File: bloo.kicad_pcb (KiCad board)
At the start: 2 copper layers, 0 parts

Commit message: feat: create PCB shape and motor placement
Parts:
- added BT1: Battery_Cell, Connector_AMASS:AMASS_XT30UPB-M_1x02_P5.0mm_Vertical, F.Cu at (27.0, 155.0)
- added BT_MH1: M2, MountingHole:MountingHole_2.2mm_M2, F.Cu at (112.9, 187.9)
- added BT_MH2: M2, MountingHole:MountingHole_2.2mm_M2, F.Cu at (112.9, 193.8)
- added BT_MH3: M2, MountingHole:MountingHole_2.2mm_M2, F.Cu at (118.5, 187.9)
- added BT_MH4: M2, MountingHole:MountingHole_2.2mm_M2, F.Cu at (118.9, 193.8)
- added C1: 0.1uF, Capacitor_SMD:C_1206_3216Metric_Pad1.33x1.80mm_HandSolder, F.Cu at (375.0, 47.8)
- added C10: 10uF(Tantalum), Capacitor_SMD:C_1206_3216Metric_Pad1.33x1.80mm_HandSolder, F.Cu at (375.0, 61.2)
- added C11: 10uF, Capacitor_SMD:C_1206_3216Metric_Pad1.33x1.80mm_HandSolder, F.Cu at (375.0, 64.6)
- added C12: 0.1uF, Capacitor_SMD:C_1206_3216Metric_Pad1.33x1.80mm_HandSolder, F.Cu at (381.0, 47.8)
- added C13: 0.1uF, Capacitor_SMD:C_1206_3216Metric_Pad1.33x1.80mm_HandSolder, F.Cu at (381.0, 51.2)
- added C14: 1uF, Capacitor_SMD:C_1206_3216Metric_Pad1.33x1.80mm_HandSolder, F.Cu at (381.0, 54.5)
- added C15: 1uF, Capacitor_SMD:C_1206_3216Metric_Pad1.33x1.80mm_HandSolder, F.Cu at (381.0, 57.9)
- added C16: 100uF, Capacitor_THT:CP_Radial_D6.3mm_P2.50mm, F.Cu at (39.3, 255.5)
- added C17: 1uF, Capacitor_SMD:C_1206_3216Metric_Pad1.33x1.80mm_HandSolder, F.Cu at (381.0, 61.2)
- added C18: 1uF, Capacitor_SMD:C_1206_3216Metric_Pad1.33x1.80mm_HandSolder, F.Cu at (381.0, 64.6)
- added C19: 0.1uF, Capacitor_SMD:C_1206_3216Metric_Pad1.33x1.80mm_HandSolder, F.Cu at (387.5, 42.1)
- added C2: 100uF, Capacitor_THT:CP_Radial_D6.3mm_P2.50mm, F.Cu at (33.3, 238.5)
- added C20: 1uF, Capacitor_SMD:C_1206_3216Metric_Pad1.33x1.80mm_HandSolder, F.Cu at (387.5, 45.4)
- added C21: 1uF, Capacitor_SMD:C_1206_3216Metric_Pad1.33x1.80mm_HandSolder, F.Cu at (387.5, 48.8)
- added C22: 0.1uF, Capacitor_SMD:C_1206_3216Metric_Pad1.33x1.80mm_HandSolder, F.Cu at (387.5, 52.1)
- added C25: 10nF, Capacitor_SMD:C_1206_3216Metric_Pad1.33x1.80mm_HandSolder, F.Cu at (387.5, 55.5)
- added C3: 1uF, Capacitor_SMD:C_1206_3216Metric_Pad1.33x1.80mm_HandSolder, F.Cu at (375.0, 51.2)
- added C4: 0.1uF, Capacitor_SMD:C_1206_3216Metric_Pad1.33x1.80mm_HandSolder, F.Cu at (375.0, 54.5)
- added C5: 100nF, Capacitor_SMD:C_0603_1608Metric, F.Cu at (275.0, 33.0)
- added C6: 47µF, Capacitor_SMD:C_1206_3216Metric, F.Cu at (316.8, 64.0)
- added C7: 12pF, Capacitor_SMD:C_0603_1608Metric_Pad1.08x0.95mm_HandSolder, F.Cu at (311.8, 63.6)
- added C8: 12pF, Capacitor_SMD:C_0603_1608Metric_Pad1.08x0.95mm_HandSolder, F.Cu at (311.8, 66.1)
- added C9: 10uF, Capacitor_SMD:C_1206_3216Metric_Pad1.33x1.80mm_HandSolder, F.Cu at (375.0, 57.9)
- added D0: SFH4545, MM_Library:Emitter, F.Cu at (121.2, 69.9)
- added D1: SFH4545, MM_Library:Emitter, F.Cu at (141.2, 66.4)
- added D2: SFH4545, MM_Library:Emitter, F.Cu at (154.7, 69.4)
- added D3: SFH4545, MM_Library:Emitter, F.Cu at (110.2, 85.4)
- added D4: LED, LED_SMD:LED_0805_2012Metric_Pad1.15x1.40mm_HandSolder, F.Cu at (185.4, 246.0)
- added D5: LED, LED_SMD:LED_0805_2012Metric_Pad1.15x1.40mm_HandSolder, F.Cu at (185.4, 249.0)
- added D6: LED, LED_SMD:LED_0805_2012Metric_Pad1.15x1.40mm_HandSolder, F.Cu at (185.4, 252.1)
- added D7: 1SS389,L3F, Diode_SMD:D_SOD-523, F.Cu at (64.6, 276.7)
- added D9: 1SS389,L3F, Diode_SMD:D_SOD-523, F.Cu at (64.6, 279.1)
- added J5: SWD_Header, Connector_PinHeader_2.54mm:PinHeader_1x05_P2.54mm_Vertical, F.Cu at (146.5, 272.3)
- added JP4: Jumper_2_Open, Jumper:SolderJumper-2_P1.3mm_Bridged_Pad1.0x1.5mm, F.Cu at (275.1, 30.0)
- added M1: M1_Conn_Alt, Connector_JST:JST_SH_BM06B-SRSS-TB_1x06-1MP_P1.00mm_Vertical, F.Cu at (321.2, 207.7)
- added M2: M2_Conn_Alt, Connector_JST:JST_SH_BM06B-SRSS-TB_1x06-1MP_P1.00mm_Vertical, F.Cu at (329.7, 247.2)
- added M_MH1: M2, MM_Library:Motor_mouse, F.Cu at (193.9, 149.0)
- added M_MH2: M2, MM_Library:Motor_mouse, F.Cu at (205.8, 149.0)
- added Q0: TEFT4300, MM_Library:Emitter, F.Cu at (181.2, 45.9)
- added Q1: TEFT4300, MM_Library:Emitter, F.Cu at (196.7, 32.2)
- added Q10: Q_NMOS_GSD, Package_TO_SOT_SMD:SOT-23, F.Cu at (322.9, 56.5)
- added Q11: Q_NMOS_GSD, Package_TO_SOT_SMD:SOT-23, F.Cu at (322.9, 61.0)
- added Q12: Q_NMOS_GSD, Package_TO_SOT_SMD:SOT-23, F.Cu at (322.9, 65.4)
- added Q2: TEFT4300, MM_Library:Emitter, F.Cu at (218.2, 20.9)
- added Q3: TEFT4300, MM_Library:Emitter, F.Cu at (168.2, 55.4)
- added Q9: Q_NMOS_GSD, Package_TO_SOT_SMD:SOT-23, F.Cu at (322.9, 52.0)
- added R1: 1.8K, Resistor_SMD:R_1206_3216Metric_Pad1.30x1.75mm_HandSolder, F.Cu at (375.0, 21.3)
- added R10: 10K, Resistor_SMD:R_1206_3216Metric_Pad1.30x1.75mm_HandSolder, F.Cu at (380.9, 24.6)
- added R12: 47K, Resistor_SMD:R_1206_3216Metric_Pad1.30x1.75mm_HandSolder, F.Cu at (380.9, 27.9)
- added R13: 47K, Resistor_SMD:R_1206_3216Metric_Pad1.30x1.75mm_HandSolder, F.Cu at (380.9, 31.3)
- added R14: 47K, Resistor_SMD:R_1206_3216Metric_Pad1.30x1.75mm_HandSolder, F.Cu at (380.9, 34.6)
- added R15: 47K, Resistor_SMD:R_1206_3216Metric_Pad1.30x1.75mm_HandSolder, F.Cu at (380.9, 37.9)
- added R16: 47K, Resistor_SMD:R_1206_3216Metric_Pad1.30x1.75mm_HandSolder, F.Cu at (380.9, 41.2)
- added R17: 47K, Resistor_SMD:R_1206_3216Metric_Pad1.30x1.75mm_HandSolder, F.Cu at (380.9, 44.5)
- added R19: 750, Resistor_SMD:R_1206_3216Metric_Pad1.30x1.75mm_HandSolder, F.Cu at (386.9, 21.3)
- added R2: 1.8K, Resistor_SMD:R_1206_3216Metric_Pad1.30x1.75mm_HandSolder, F.Cu at (375.0, 24.6)
- added R20: 75, Resistor_SMD:R_1206_3216Metric_Pad1.30x1.75mm_HandSolder, F.Cu at (386.9, 24.6)
- added R21: 75, Resistor_SMD:R_1206_3216Metric_Pad1.30x1.75mm_HandSolder, F.Cu at (386.9, 27.9)
- added R22: 20K, Resistor_SMD:R_1206_3216Metric_Pad1.30x1.75mm_HandSolder, F.Cu at (386.9, 31.3)
- added R23: 10K, Resistor_SMD:R_1206_3216Metric_Pad1.30x1.75mm_HandSolder, F.Cu at (386.9, 34.6)
- added R24: 47K, Resistor_SMD:R_1206_3216Metric_Pad1.30x1.75mm_HandSolder, F.Cu at (386.9, 37.9)
- added R3: 1.8K, Resistor_SMD:R_1206_3216Metric_Pad1.30x1.75mm_HandSolder, F.Cu at (375.0, 27.9)
- added R4: 1.8K, Resistor_SMD:R_1206_3216Metric_Pad1.30x1.75mm_HandSolder, F.Cu at (375.0, 31.3)
- added R5: 36, Resistor_SMD:R_1206_3216Metric_Pad1.30x1.75mm_HandSolder, F.Cu at (375.0, 34.6)
- added R6: 36, Resistor_SMD:R_1206_3216Metric_Pad1.30x1.75mm_HandSolder, F.Cu at (375.0, 37.9)
- added R7: 36, Resistor_SMD:R_1206_3216Metric_Pad1.30x1.75mm_HandSolder, F.Cu at (375.0, 41.2)
- added R8: 36, Resistor_SMD:R_1206_3216Metric_Pad1.30x1.75mm_HandSolder, F.Cu at (375.0, 44.5)
- added R9: 47K, Resistor_SMD:R_1206_3216Metric_Pad1.30x1.75mm_HandSolder, F.Cu at (380.9, 21.3)
- added S1: EG1218, MM_Library:MM Switch, F.Cu at (26.0, 183.8)
- added S2: SKRPABE010, MM_Library:SW4_SKRPABE010_ALPS, F.Cu at (229.4, 265.4)
- added S3: SKRPABE010, MM_Library:SW4_SKRPABE010_ALPS, F.Cu at (80.1, 278.5)
- added S5: SKRPABE010, MM_Library:SW4_SKRPABE010_ALPS, F.Cu at (285.5, 274.0)
- added SK1: M2, MountingHole:MountingHole_2.2mm_M2, F.Cu at (124.8, 187.9)
- added SK2: M2, MountingHole:MountingHole_2.2mm_M2, F.Cu at (124.8, 193.8)
- added SK3: M2, MountingHole:MountingHole_2.2mm_M2, F.Cu at (130.8, 187.9)
- added SK4: M2, MountingHole:MountingHole_2.2mm_M2, F.Cu at (130.8, 193.8)
- added TP1: V_EXT_TP, Connector_PinHeader_2.54mm:PinHeader_1x01_P2.54mm_Vertical, F.Cu at (36.3, 199.9)
- added TP2: GND_TP, Connector_PinHeader_2.54mm:PinHeader_1x01_P2.54mm_Vertical, F.Cu at (36.3, 204.5)
- added TP3: TP_5V, Connector_PinHeader_2.54mm:PinHeader_1x01_P2.54mm_Vertical, F.Cu at (40.9, 199.9)
- added TP4: TP_3V3, Connector_PinHeader_2.54mm:PinHeader_1x01_P2.54mm_Vertical, F.Cu at (40.9, 204.5)
- added TP5: GND_TP, Connector_PinHeader_2.54mm:PinHeader_1x01_P2.54mm_Vertical, F.Cu at (45.5, 199.9)
- added TP6: GND_TP, Connector_PinHeader_2.54mm:PinHeader_1x01_P2.54mm_Vertical, F.Cu at (45.5, 204.5)
- added U1: YAAJ_BluePill_SWD_Breakout, MM_Library:STM32F103, F.Cu at (256.1, 260.0)
- added U2: L293D, Package_DIP:DIP-16_W7.62mm, F.Cu at (370.9, 209.8)
- added U3: LM1085-5.0, MM_Library:5V Voltage Reg, F.Cu at (99.3, 59.1)
- added U4: NCP161ASN330T1G, Package_TO_SOT_SMD:SOT-23-5, F.Cu at (269.8, 30.2)
- added U5: BC832, MM_Library:XCVR_BC832, F.Cu at (176.8, 272.9)
- added Y1: ABS07-32.768KHZ-T, MM_Library:CAP_ABS07-32.768KHZ-T_ABR, F.Cu at (270.0, 33.9)
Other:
- board outline added: 465.1 x 141 mm

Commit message: feat: change pcb shape for more space, and group components
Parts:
- moved R21 401.8 mm to (23.6, 199.5)
- moved R20 398.5 mm to (30.1, 202.0)
- moved R19 396.5 mm to (36.0, 206.0)
- moved C2 381.5 mm to (365.0, 50.0)
- moved S1 377.7 mm to (377.6, 46.1)
- moved BT1 373.7 mm to (386.5, 53.0)
- moved TP1 367.5 mm to (366.0, 37.5)
- moved C16 364.2 mm to (357.0, 77.5)
- moved TP2 357.6 mm to (365.0, 63.5)
- moved TP6 356.6 mm to (376.0, 70.5)
- moved TP5 349.6 mm to (370.5, 71.0)
- moved C3 344.7 mm to (38.6, 126.0), turned to 180 degrees
- moved R10 343.2 mm to (139.0, 268.0)
- moved D7 341.1 mm to (385.0, 159.7), turned to 90 degrees
- moved U2 339.4 mm to (45.5, 113.0), turned to -90 degrees
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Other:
- board size 465.1 x 141 mm -> 205 x 115 mm
- board text added: "Bluetooth"
- board text added: "Buttons"
- board text added: "Emitter/Reciever"
- board text added: "Led"
- board text added: "Motor"
- board text added: "Power"

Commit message: feat: expand pcb area and add details
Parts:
- moved U1 110.6 mm to (198.7, 122.7)
- moved D0 26.9 mm to (173.8, 81.1), turned to 180 degrees
- moved Q3 23.9 mm to (183.8, 78.6), turned to 180 degrees
- moved D3 21.4 mm to (189.3, 80.8), turned to 180 degrees
- moved Q0 21.3 mm to (179.3, 78.6), turned to 180 degrees
- moved D2 9.88 mm to (186.7, 67.8), turned to 135 degrees
- moved Q2 9.43 mm to (183.7, 63.1), turned to 135 degrees
- moved D1 7.01 mm to (174.8, 65.8), turned to -135 degrees
- moved Q1 6.21 mm to (178.3, 61.5), turned to -135 degrees
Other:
- board size 205 x 115 mm -> 216 x 118.2 mm

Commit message: feat: add emitter / receiver components and traces
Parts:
- moved R4 127.0 mm to (231.5, 117.5), turned to 90 degrees
- moved C14 125.9 mm to (197.0, 140.5), turned to 0 degrees
- moved R16 123.0 mm to (232.0, 130.0), turned to 90 degrees
- moved C21 121.7 mm to (203.0, 137.0)
- moved C20 120.1 mm to (197.0, 137.0), turned to 0 degrees
- moved C15 118.5 mm to (203.0, 140.5), turned to 180 degrees
- moved R8 116.6 mm to (236.0, 126.5), turned to 180 degrees
- moved Q12 99.7 mm to (236.0, 129.9), turned to 90 degrees
- moved R3 96.4 mm to (226.5, 109.5), turned to 90 degrees
- moved R15 92.0 mm to (206.0, 109.0), turned to 180 degrees
- moved R14 82.6 mm to (194.0, 109.0), turned to 180 degrees
- moved R13 79.4 mm to (168.0, 130.5), turned to -90 degrees
- moved R7 75.4 mm to (207.5, 105.0), turned to 90 degrees
- moved R1 70.0 mm to (169.0, 117.5), turned to 90 degrees
- moved R2 69.4 mm to (173.5, 109.5), turned to -90 degrees
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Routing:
- net AGND: track 0.00 -> 134.6 mm, vias 0 -> 3
- net +3.3VA: track 0.00 -> 134.6 mm
- net +5V: track 0.00 -> 108.6 mm
- net EMIT_3: track 0.00 -> 68.4 mm
- net EMIT_4: track 0.00 -> 44.1 mm
- net RECEIV_3: track 0.00 -> 41.4 mm
- net GND: track 0.00 -> 37.0 mm
- net RECEIV_1: track 0.00 -> 29.6 mm
- net EMIT_2: track 0.00 -> 26.9 mm
- net RECEIV_4: track 0.00 -> 25.7 mm
- net RECEIV_2: track 0.00 -> 24.7 mm
- net EMIT_1: track 0.00 -> 13.6 mm
- net Net-(D2-K): track 0.00 -> 7.07 mm
- net Net-(D0-K): track 0.00 -> 3.74 mm
- net Net-(Q11-D): track 0.00 -> 3.57 mm
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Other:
- outline, holes or cut-outs redrawn

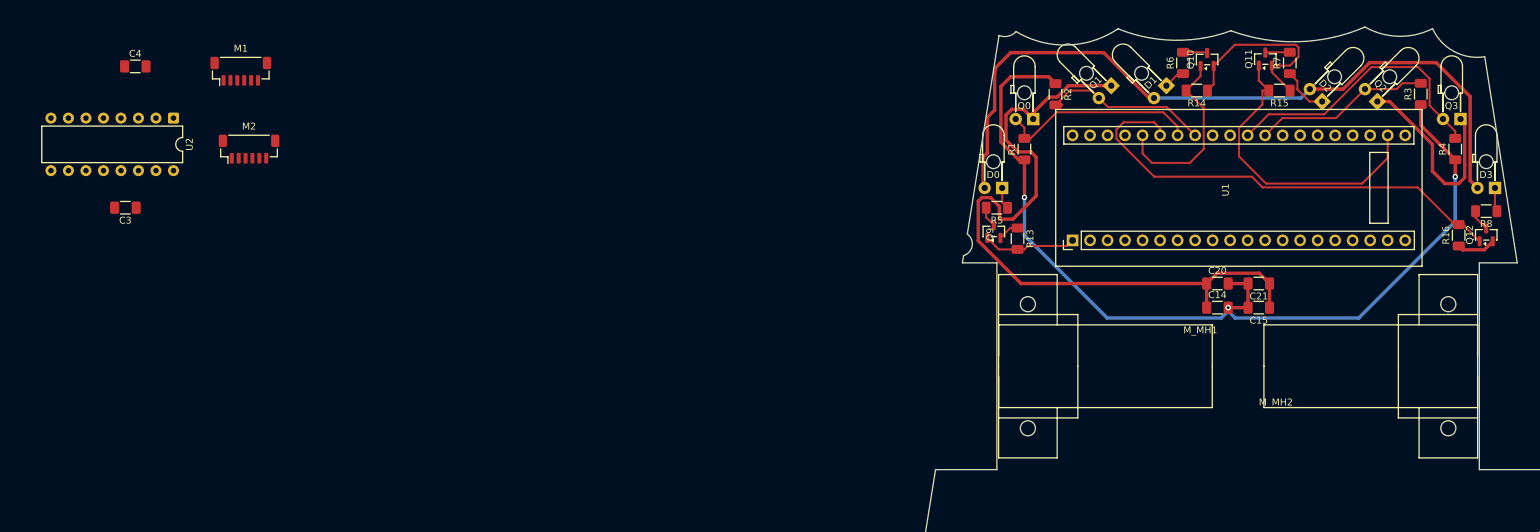
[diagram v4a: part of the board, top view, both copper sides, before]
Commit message: feat: add motor components and traces
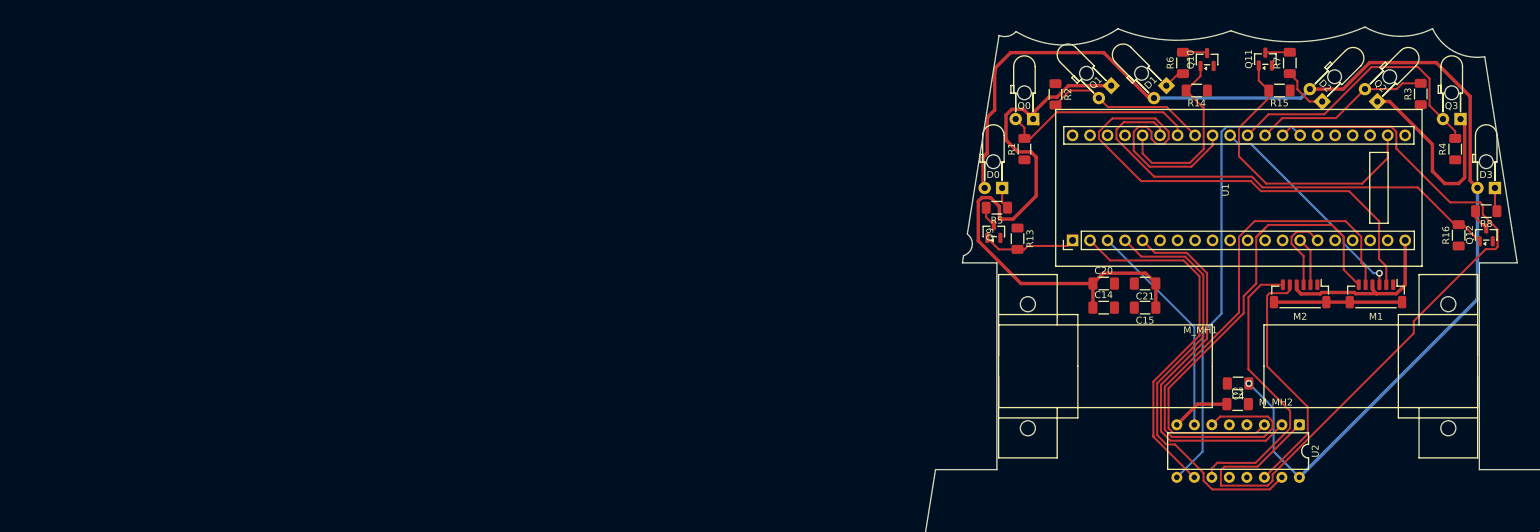
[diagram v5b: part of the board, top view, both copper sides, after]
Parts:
- moved U2 169.3 mm to (208.9, 157.5)
- moved M1 167.8 mm to (220.0, 138.5), turned to 180 degrees
- moved C4 166.5 mm to (200.0, 151.5), turned to 180 degrees
- moved C3 163.9 mm to (199.9, 154.5), turned to 0 degrees
- moved M2 153.9 mm to (209.0, 138.5), turned to 180 degrees
- moved C14 16.5 mm to (180.5, 140.5)
- moved C15 16.5 mm to (186.5, 140.5)
- moved C20 16.5 mm to (180.5, 137.0)
- moved C21 16.5 mm to (186.5, 137.0)
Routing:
- net AGND: track 134.6 -> 0.00 mm, vias 3 -> 0
- net M1_SPD: track 0.00 -> 115.1 mm
- net M1_ENC_B: track 0.00 -> 94.3 mm
- net M1_OUT_2: track 0.00 -> 86.5 mm
- net M1_OUT_1: track 0.00 -> 73.2 mm
- net +5V: track 108.6 -> 177.9 mm, vias 0 -> 1
- net M2_SPD: track 0.00 -> 65.1 mm
- net M2_BACK: track 0.00 -> 62.2 mm
- net M1_FWD: track 0.00 -> 56.1 mm
- net M2_FWD: track 0.00 -> 52.7 mm
- net +3V3: track 0.00 -> 42.9 mm
- net M2_OUT_1: track 0.00 -> 42.4 mm
- net GND: track 37.0 -> 0.00 mm
- net M2_OUT_2: track 0.00 -> 35.8 mm
- net M1_ENC_A: track 0.00 -> 32.2 mm, vias 0 -> 1
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
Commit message: feat: create Bluetooth components and traces
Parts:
- moved C7 145.4 mm to (227.5, 163.5), turned to 180 degrees
- moved U5 145.4 mm to (220.3, 161.2)
- moved J5 145.2 mm to (213.0, 157.5)
- moved Y1 140.0 mm to (228.0, 166.0), turned to 180 degrees
- moved C5 139.9 mm to (233.0, 171.0), turned to 0 degrees
- moved C6 138.6 mm to (234.0, 165.5)
- moved C8 138.3 mm to (227.0, 168.5)
- moved R10 137.6 mm to (234.0, 168.5), turned to 180 degrees
- moved C20 2.00 mm to (180.5, 139.0)
- moved C21 2.00 mm to (186.5, 139.0)
- moved C14 1.00 mm to (180.5, 141.5)
- moved C15 1.00 mm to (186.5, 141.5)
- moved Q12 0.56 mm to (236.0, 130.5)
- moved R8 0.50 mm to (236.0, 127.0)
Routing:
- net BLE_SPI_MOSI: track 0.00 -> 153.1 mm
- net BLE_SPI_MISO: track 0.00 -> 148.5 mm
- net BLE_SPI_SCK: track 0.00 -> 128.9 mm
- net USART1_RX: track 0.00 -> 105.3 mm
- net BLE_LED: track 0.00 -> 97.3 mm
- net USART1_TX: track 0.00 -> 96.9 mm
- net BLE_STATE: track 0.00 -> 88.8 mm
- net M1_SPD: track 115.1 -> 43.0 mm
- net +3V3: track 42.9 -> 73.7 mm
- net M1_OUT_1: track 73.2 -> 46.5 mm, vias 0 -> 1
- net BT_RESET: track 0.00 -> 25.0 mm, vias 0 -> 2
- net Net-(U5-P00/XL1): track 0.00 -> 11.6 mm
- net M1_ENC_A: track 32.2 -> 39.5 mm
- net Net-(U5-P01/XL2): track 0.00 -> 5.78 mm
- net M2_ENC_B: track 7.06 -> 12.5 mm
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
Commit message: refactor: move Bluetooth components for better trace management
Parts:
- moved C6 68.0 mm to (166.0, 166.5), turned to 180 degrees
- moved R10 67.5 mm to (166.5, 169.0), turned to 0 degrees
- moved C5 62.5 mm to (170.5, 169.0)
- moved C8 59.2 mm to (168.0, 164.0)
- moved Y1 57.0 mm to (171.0, 166.5), turned to 0 degrees
- moved C7 56.0 mm to (171.5, 164.0), turned to 0 degrees
- moved U5 40.9 mm to (179.4, 162.1), turned to 180 degrees
- moved J5 37.4 mm to (177.4, 169.0), turned to 90 degrees
- moved S1 4.25 mm to (373.4, 46.1)
- moved U4 4.25 mm to (337.1, 53.5)
- moved BT1 4.25 mm to (382.3, 53.0)
- moved C1 4.25 mm to (365.7, 58.5)
- moved C10 4.25 mm to (350.2, 65.5)
- moved C11 4.25 mm to (333.8, 76.5)
- moved C12 4.25 mm to (335.7, 69.5)
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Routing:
- net USART1_RX: track 105.3 -> 41.7 mm, vias 0 -> 1
- net BLE_SPI_MOSI: track 153.1 -> 114.2 mm
- net BLE_SPI_MISO: track 148.5 -> 113.4 mm
- net BLE_SPI_SCK: track 128.9 -> 108.9 mm
- net +3V3: track 73.7 -> 59.7 mm, vias 0 -> 1
- net USART1_TX: track 96.9 -> 106.8 mm
- net BLE_STATE: track 88.8 -> 80.5 mm, vias 0 -> 1
- net BT_RESET: track 25.0 -> 33.0 mm, vias 2 -> 1
- net M2_ENC_B: track 12.5 -> 7.06 mm, vias 0 -> 1
- net BT_SWDIO: track 3.77 -> 8.78 mm
- net BT_SWDCLK: track 4.36 -> 8.27 mm
- net M1_OUT_2: track 81.2 -> 83.7 mm
- net Net-(U5-P01/XL2): track 5.78 -> 6.81 mm
- net BLE_LED: track 97.3 -> 98.3 mm, vias 0 -> 1
- net M2_BACK: track 62.2 -> 61.4 mm
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
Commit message: feat: add LED components and traces
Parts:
- moved D6 187.4 mm to (196.5, 134.5), turned to -90 degrees
- moved D5 185.9 mm to (199.0, 134.5), turned to -90 degrees
- moved R21 182.4 mm to (196.5, 139.0), turned to -90 degrees
- moved R20 179.5 mm to (199.0, 139.0), turned to -90 degrees
- moved D4 178.2 mm to (194.0, 134.5), turned to -90 degrees
- moved R19 170.6 mm to (194.0, 139.0), turned to -90 degrees
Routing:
- net USART1_TX: track 106.8 -> 42.4 mm, vias 0 -> 1
- net +3V3: track 59.7 -> 71.3 mm, vias 1 -> 3
- net BLE_SPI_MOSI: track 114.2 -> 108.2 mm
- net BLE_SPI_MISO: track 113.4 -> 107.7 mm
- net M2_ENC_B: track 7.06 -> 12.5 mm, vias 1 -> 0
- net BLE_SPI_SCK: track 108.9 -> 104.7 mm
- net M2_BACK: track 61.4 -> 57.4 mm
- net M1_FWD: track 56.3 -> 52.3 mm
- net M2_FWD: track 52.4 -> 48.8 mm
- net LED_RED: track 0.00 -> 2.83 mm
- net LED_BLUE: track 0.00 -> 2.82 mm
- net LED_GREEN: track 0.00 -> 2.80 mm
- net Net-(D6-A): track 0.00 -> 1.92 mm
- net Net-(D5-A): track 0.00 -> 1.92 mm
- net Net-(D4-A): track 0.00 -> 1.92 mm
